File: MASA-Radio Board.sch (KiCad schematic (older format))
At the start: 50 parts, among them IC1 FAN4010IL6X_F113, IC2 FAN4010IL6X_F113, J1 Conn_01x02, J2 Conn_01x02_Male, J3 Conn_01x02_Male, J4 Conn_01x03_Male, J5 Conn_01x06, J6 SC_19-20, J7 Conn_01x06, J8 Conn_01x02, J9 UJ2-MBH-1-SMT-TR, U1 MP5077GG-Z, U2 BL654PA, U3 MIC5504-3.3YM5, U4 MP5077GG-Z

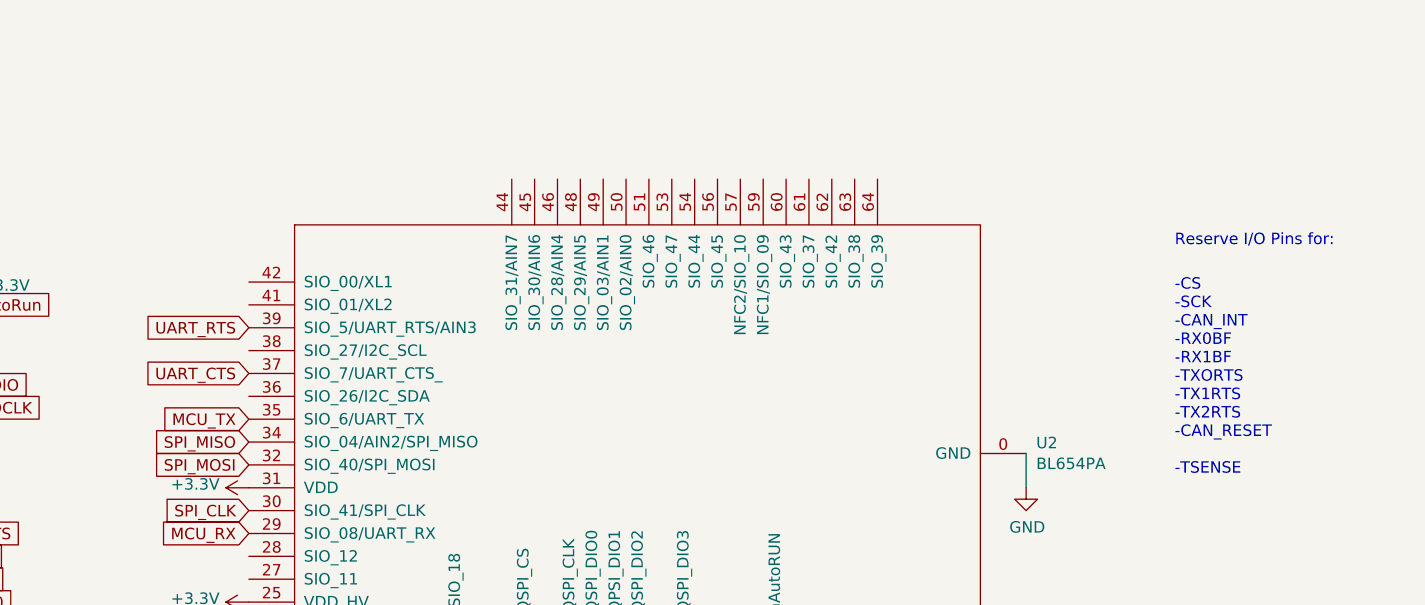
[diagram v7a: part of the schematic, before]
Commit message: fixed tsense
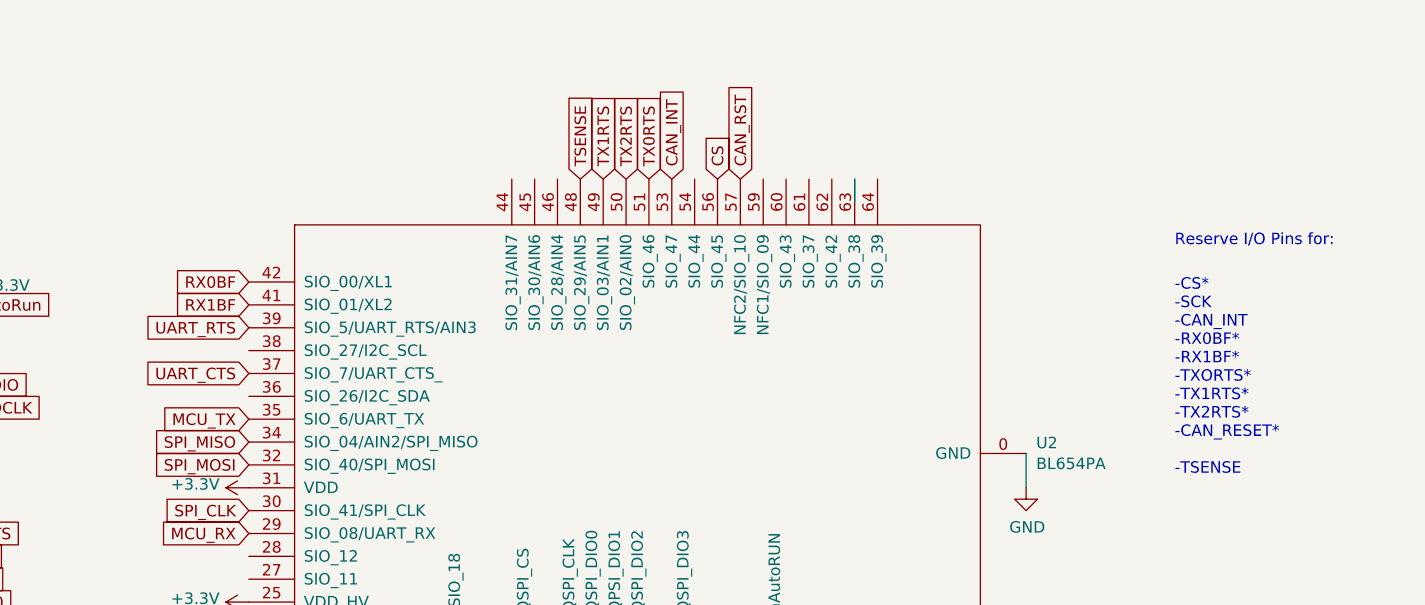
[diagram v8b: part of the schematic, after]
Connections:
- net CAN_INT: now also U2.53 (SIO_47)
- net CAN_RST: now also U2.57 (NFC2/SIO_10)
- net CS: now also U2.56 (SIO_45)
- net RX0BF: now also U2.42 (SIO_00/XL1)
- net RX1BF: now also U2.41 (SIO_01/XL2)
- net TSENSE: now also U2.48 (SIO_29/AIN5)
- net TX0RTS: now also U2.51 (SIO_46)
- net TX1RTS: now also U2.49 (SIO_03/AIN1)
- net TX2RTS: now also U2.50 (SIO_02/AIN0)
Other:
- note added: "-CS*\n-SCK\n-CAN_INT\n-RX0BF*\n-RX1BF*\n-TXORTS*\n-TX1RTS*\n-TX2RTS*\n-CAN_RESET*\n\n-TSENSE"
- note removed: "-CS\n-SCK\n-CAN_INT\n-RX0BF\n-RX1BF\n-TXORTS\n-TX1RTS\n-TX2RTS\n-CAN_RESET\n\n-TSENSE"
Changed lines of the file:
@@
 Reserve I/O Pins for:
 Text Notes 15500 3850 0    50   ~ 0
--CS\n-SCK\n-CAN_INT\n-RX0BF\n-RX1BF\n-TXORTS\n-TX1RTS\n-TX2RTS\n-CAN_RESET\n\n-TSENSE
+-CS*\n-SCK\n-CAN_INT\n-RX0BF*\n-RX1BF*\n-TXORTS*\n-TX1RTS*\n-TX2RTS*\n-CAN_RESET*\n\n-TSENSE
 Wire Wire Line
 	4950 4150 5550 4150
@@
 USB_D+
 $Comp
-L power:+3.3V #PWR?
+L power:+3.3V #PWR0101
 U 1 1 5E65F90C
 P 10150 3000
-F 0 "#PWR?" H 10150 2850 50  0001 C CNN
+F 0 "#PWR0101" H 10150 2850 50  0001 C CNN
 F 1 "+3.3V" V 10165 3128 50  0000 L CNN
 F 2 "" H 10150 3000 50  0001 C CNN
@@
 	0    1    1    0
 $EndComp
+Text GLabel 13600 2550 1    50   Input ~ 0
+CAN_RST
+Text GLabel 13500 2550 1    50   Input ~ 0
+CS
+Text GLabel 11450 3100 0    50   Input ~ 0
+RX1BF
+Text GLabel 11450 3000 0    50   Input ~ 0
+RX0BF
+Text GLabel 13200 2550 1    50   Input ~ 0
+TX0RTS
+Text GLabel 13100 2550 1    50   Input ~ 0
+TX2RTS
+Text GLabel 13000 2550 1    50   Input ~ 0
+TX1RTS
+Text GLabel 13300 2550 1    50   Input ~ 0
+CAN_INT
+Wire Wire Line
+	14100 2550 14100 2650
+Text GLabel 12900 2550 1    50   Input ~ 0
+TSENSE
 $EndSCHEMATC
